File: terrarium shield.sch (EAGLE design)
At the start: 17 parts

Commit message: Connected the other two GND pins to the ground pour.
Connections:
- net GND: now also U$1.GND, U$1.GND1
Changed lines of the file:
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@@
 <part name="R2" library="tjw" deviceset="RESISTOR_US_THM" device="" value="10k"/>
 <part name="RESET" library="tjw" deviceset="TACTILE_BUTTON_THM" device=""/>
+<part name="GND16" library="supply1" deviceset="GND" device=""/>
 </parts>
 <sheets>
@@
 <instance part="R2" gate="G$1" x="50.8" y="25.4"/>
 <instance part="RESET" gate="G$1" x="33.02" y="35.56"/>
+<instance part="GND16" gate="1" x="15.24" y="109.22"/>
 </instances>
 <busses>
@@
 <pinref part="GND13" gate="1" pin="GND"/>
 <wire x1="63.5" y1="50.8" x2="60.96" y2="50.8" width="0.1524" layer="91"/>
+<pinref part="U$1" gate="G$1" pin="GND1"/>
+<wire x1="66.04" y1="58.42" x2="66.04" y2="50.8" width="0.1524" layer="91"/>
+<wire x1="66.04" y1="50.8" x2="60.96" y2="50.8" width="0.1524" layer="91"/>
+<junction x="60.96" y="50.8"/>
 </segment>
 <segment>
@@
 <wire x1="-78.74" y1="190.5" x2="-78.74" y2="182.88" width="0.1524" layer="91"/>
 </segment>
+<segment>
+<pinref part="U$1" gate="G$1" pin="GND"/>
+<wire x1="45.72" y1="119.38" x2="45.72" y2="127" width="0.1524" layer="91"/>
+<wire x1="45.72" y1="127" x2="15.24" y2="127" width="0.1524" layer="91"/>
+<pinref part="GND16" gate="1" pin="GND"/>
+<wire x1="15.24" y1="127" x2="15.24" y2="111.76" width="0.1524" layer="91"/>
+</segment>
 </net>

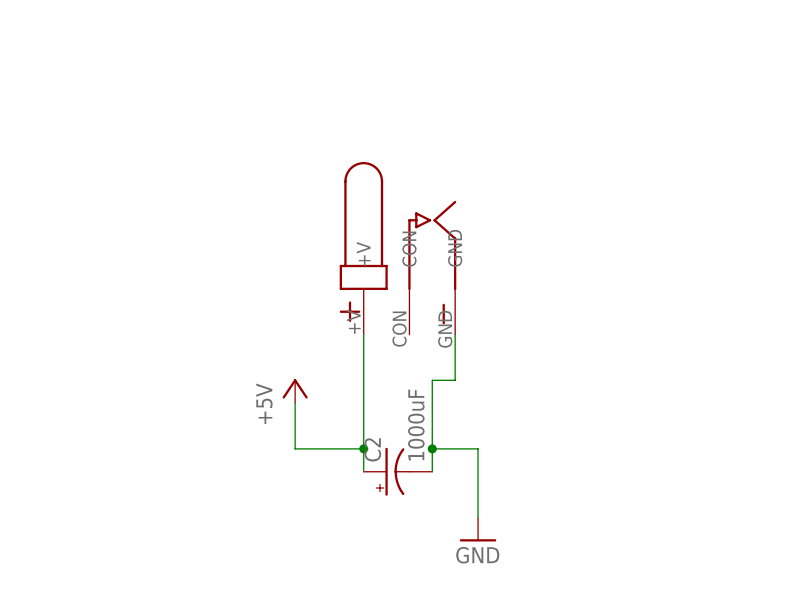
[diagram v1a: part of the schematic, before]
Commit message: Removed DC jack. Will get power from VIN.
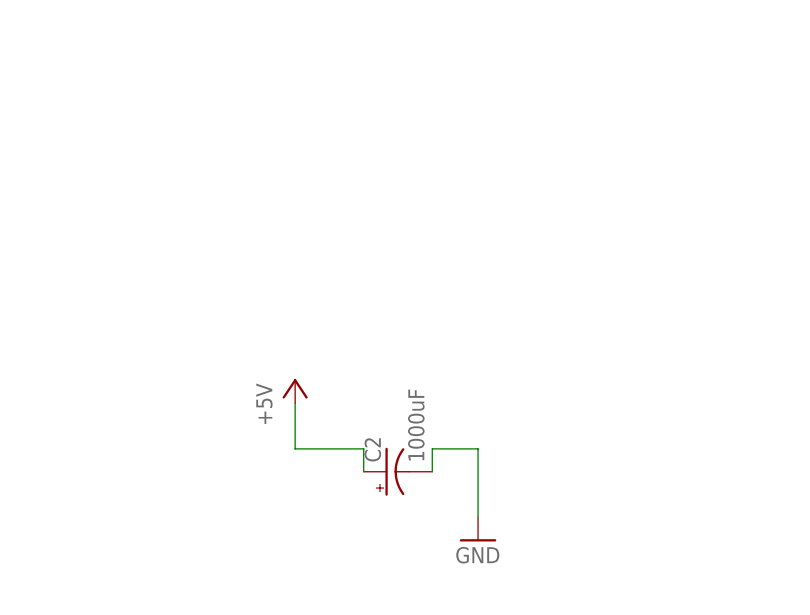
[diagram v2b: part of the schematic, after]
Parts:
- removed 5V_DC: 2.1MM_DC_JACK, tjw:2.1MM_DC_JACK
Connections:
- net +5V: no longer 5V_DC.+V
- net GND: no longer 5V_DC.GND
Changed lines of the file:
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@@
 <part name="GND15" library="supply1" deviceset="GND" device=""/>
 <part name="U$1" library="tjw" deviceset="ARDUINO_UNO_R3" device=""/>
-<part name="5V_DC" library="tjw" deviceset="2.1MM_DC_JACK" device=""/>
 <part name="TEMP_HUM" library="tjw" deviceset="MOLEX_3PIN_VERT_THM" device=""/>
 <part name="LED0" library="tjw" deviceset="MOLEX_3PIN_VERT_THM" device=""/>
@@
 <instance part="GND15" gate="1" x="15.24" y="25.4"/>
 <instance part="U$1" gate="G$1" x="30.48" y="63.5"/>
-<instance part="5V_DC" gate="G$1" x="-33.02" y="63.5" rot="MR270"/>
 <instance part="TEMP_HUM" gate="G$1" x="-78.74" y="200.66"/>
 <instance part="LED0" gate="G$1" x="-48.26" y="200.66"/>
@@
 <wire x1="-25.4" y1="38.1" x2="-25.4" y2="45.72" width="0.1524" layer="91"/>
 <wire x1="-25.4" y1="45.72" x2="-30.48" y2="45.72" width="0.1524" layer="91"/>
-<pinref part="5V_DC" gate="G$1" pin="GND"/>
-<wire x1="-27.94" y1="58.42" x2="-27.94" y2="53.34" width="0.1524" layer="91"/>
-<wire x1="-27.94" y1="53.34" x2="-30.48" y2="53.34" width="0.1524" layer="91"/>
-<wire x1="-30.48" y1="53.34" x2="-30.48" y2="45.72" width="0.1524" layer="91"/>
 <pinref part="C2" gate="G$1" pin="-"/>
 <wire x1="-30.48" y1="45.72" x2="-30.48" y2="43.18" width="0.1524" layer="91"/>
-<junction x="-30.48" y="45.72"/>
 </segment>
 <segment>
@@
 <wire x1="-45.72" y1="50.8" x2="-45.72" y2="45.72" width="0.1524" layer="91"/>
 <wire x1="-45.72" y1="45.72" x2="-38.1" y2="45.72" width="0.1524" layer="91"/>
-<pinref part="5V_DC" gate="G$1" pin="+V"/>
-<wire x1="-38.1" y1="58.42" x2="-38.1" y2="45.72" width="0.1524" layer="91"/>
 <pinref part="C2" gate="G$1" pin="+"/>
 <wire x1="-38.1" y1="45.72" x2="-38.1" y2="43.18" width="0.1524" layer="91"/>
-<junction x="-38.1" y="45.72"/>
 </segment>
 <segment>
